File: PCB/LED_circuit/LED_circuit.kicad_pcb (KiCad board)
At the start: 2 copper layers, 41 x 43 mm, 14 parts

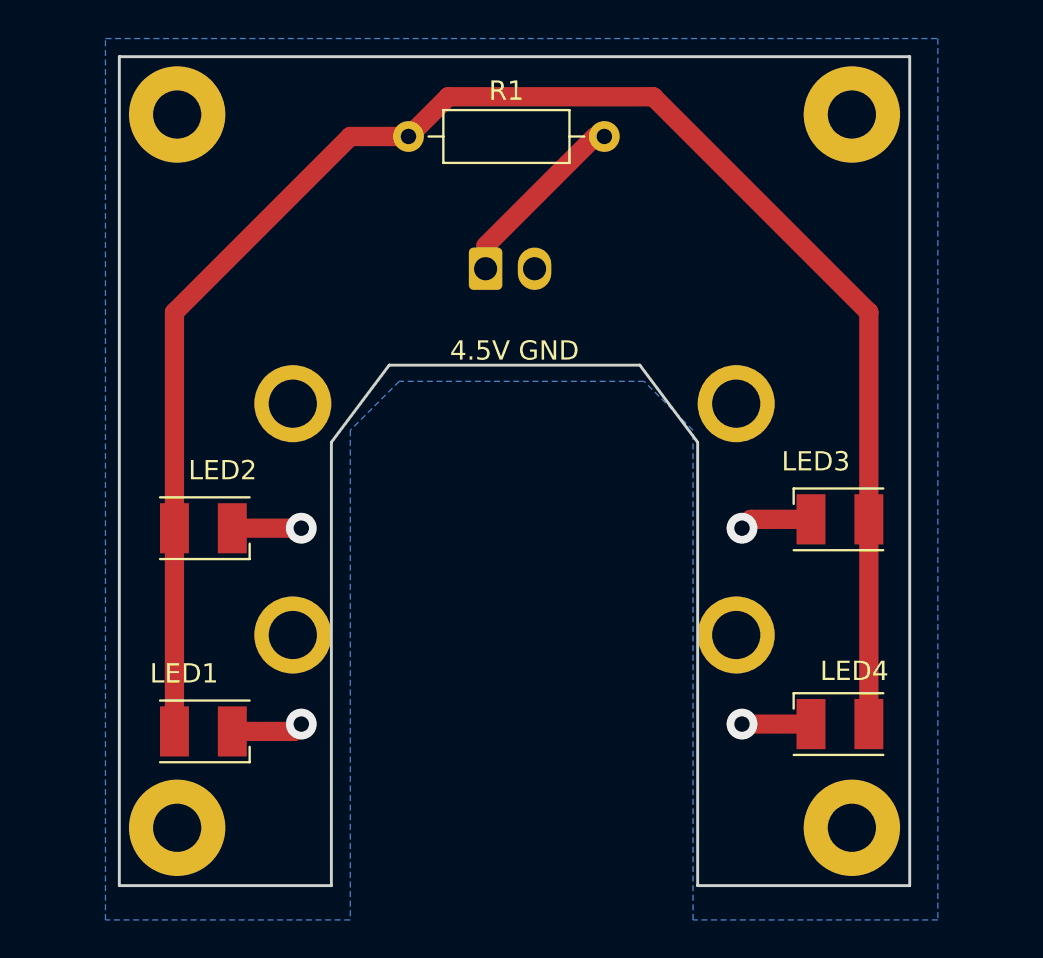
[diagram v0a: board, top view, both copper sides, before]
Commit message: Added LEDs to have the option of installing more if needed, fixed ground layer on main board to be connected everywhere, rewired pins to ease soldering
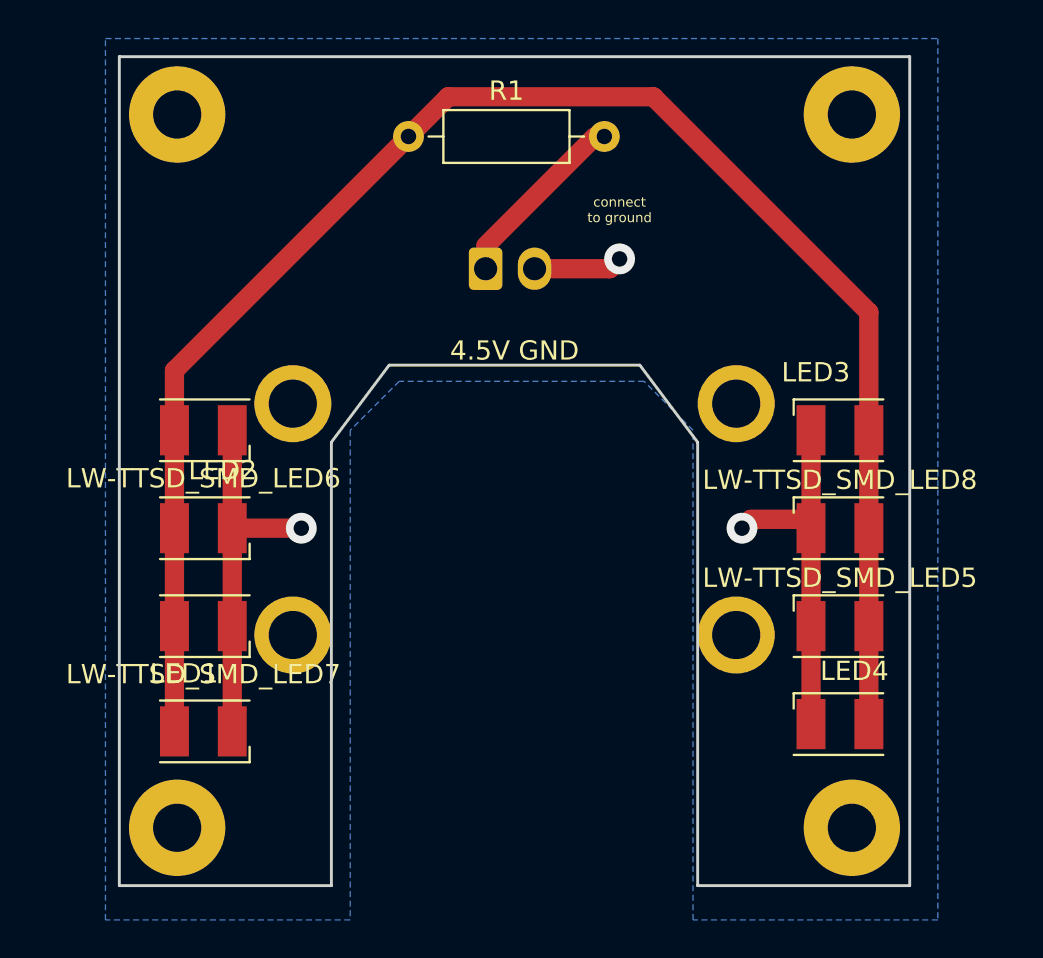
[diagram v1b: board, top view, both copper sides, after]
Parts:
- added LW-TTSD_SMD_LED5: 3.2V, LED_SMD:LED_PLCC-2, F.Cu at (119.4, 129.5)
- added LW-TTSD_SMD_LED6: 3.2V, LED_SMD:LED_PLCC-2, F.Cu at (86.4, 119.4)
- added LW-TTSD_SMD_LED7: 3.2V, LED_SMD:LED_PLCC-2, F.Cu at (86.4, 129.5)
- added LW-TTSD_SMD_LED8: 3.2V, LED_SMD:LED_PLCC-2, F.Cu at (119.4, 124.5)
- moved LED3 4.62 mm to (119.4, 119.4)
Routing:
- net Net-(Conn_01x02_Male1-Pad2): track 14.7 -> 42.8 mm, vias 4 -> 3
- net Net-(CURRENT_LIMITER_R1-Pad1): track 88.4 -> 86.6 mm
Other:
- net class Default: clearance 0.25 -> 0.5; trace_width 0.5 -> 1
- rule trace_clearance: 0.25 -> 0.5
- board text added: "connect to ground"
